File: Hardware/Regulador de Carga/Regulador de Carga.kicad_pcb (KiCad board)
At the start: 2 copper layers, 16 parts

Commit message: Actualizacion de placas
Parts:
- removed BATout1: Screw_Terminal_01x04, TerminalBlock:TerminalBlock_bornier-4_P5.08mm
- added J1: Screw_Terminal_01x05, TerminalBlock:TerminalBlock_bornier-5_P5.08mm, F.Cu at (110.5, 85.1)
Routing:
- net Net-(BATin1-Pad2): track 70.1 -> 73.4 mm
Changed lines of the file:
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@@
     (add_net "Net-(op1-Pad8)")
+  )
+  (module TerminalBlock:TerminalBlock_bornier-5_P5.08mm (layer F.Cu)
+    (at 110.49 85.09 90)
+    (descr "simple 5-pin terminal block, pitch 5.08mm, revamped version of bornier5")
+    (tags "terminal block bornier5")
+    (fp_text reference J1 (at 10.15 -4.55 90) (layer F.SilkS)
+      (effects (font (size 1 1) (thickness 0.15)))
+    )
+    (fp_text value Screw_Terminal_01x05 (at 10.15 4.6 90) (layer F.Fab)
+      (effects (font (size 1 1) (thickness 0.15)))
+    )
+    (fp_line (start 23.06 4) (end -2.74 4) (layer F.CrtYd) (width 0.05))
+    (fp_line (start 23.06 4) (end 23.06 -4) (layer F.CrtYd) (width 0.05))
+    (fp_line (start -2.74 -4) (end -2.74 4) (layer F.CrtYd) (width 0.05))
+    (fp_line (start -2.74 -4) (end 23.06 -4) (layer F.CrtYd) (width 0.05))
+    (fp_line (start -2.54 -3.81) (end -2.54 3.81) (layer F.SilkS) (width 0.12))
+    (fp_line (start 22.86 -3.81) (end 22.86 3.81) (layer F.SilkS) (width 0.12))
+    (fp_line (start -2.54 -3.81) (end 22.86 -3.81) (layer F.SilkS) (width 0.12))
+    (fp_line (start -2.54 2.54) (end 22.86 2.54) (layer F.SilkS) (width 0.12))
+    (fp_line (start -2.54 3.81) (end 22.86 3.81) (layer F.SilkS) (width 0.12))
+    (fp_line (start 22.81 -3.75) (end -2.49 -3.75) (layer F.Fab) (width 0.1))
+    (fp_line (start 22.81 3.75) (end 22.81 -3.75) (layer F.Fab) (width 0.1))
+    (fp_line (start -2.49 3.75) (end 22.81 3.75) (layer F.Fab) (width 0.1))
+    (fp_line (start -2.49 -3.75) (end -2.49 3.75) (layer F.Fab) (width 0.1))
+    (fp_line (start -2.49 2.55) (end 22.81 2.55) (layer F.Fab) (width 0.1))
+    (fp_text user %R (at 10.16 0 90) (layer F.Fab)
+      (effects (font (size 1 1) (thickness 0.15)))
+    )
+    (pad 5 thru_hole circle (at 20.32 0 90) (size 3 3) (drill 1.52) (layers *.Cu *.Mask)
+      (net 2 Earth))
+    (pad 4 thru_hole circle (at 15.24 0 90) (size 3 3) (drill 1.52) (layers *.Cu *.Mask)
+      (net 1 "Net-(BATin1-Pad2)"))
+    (pad 1 thru_hole rect (at 0 0 90) (size 3 3) (drill 1.52) (layers *.Cu *.Mask)
+      (net 2 Earth))
+    (pad 3 thru_hole circle (at 10.16 0 90) (size 3 3) (drill 1.52) (layers *.Cu *.Mask)
+      (net 1 "Net-(BATin1-Pad2)"))
+    (pad 2 thru_hole circle (at 5.08 0 90) (size 3 3) (drill 1.52) (layers *.Cu *.Mask)
+      (net 1 "Net-(BATin1-Pad2)"))
+    (model ${KISYS3DMOD}/TerminalBlock.3dshapes/TerminalBlock_bornier-5_P5.08mm.wrl
+      (offset (xyz 10.15999984741211 0 0))
+      (scale (xyz 1 1 1))
+      (rotate (xyz 0 0 0))
+    )
   )
   (module Diode_THT:D_DO-15_P12.70mm_Horizontal (layer F.Cu)
@@
     )
   )
-  (module TerminalBlock:TerminalBlock_bornier-4_P5.08mm (layer F.Cu)
-    (at 110.49 66.548 270)
-    (descr "simple 4-pin terminal block, pitch 5.08mm, revamped version of bornier4")
-    (tags "terminal block bornier4")
-    (fp_text reference BATout1 (at 19.23 0.49) (layer F.SilkS)
-      (effects (font (size 1 1) (thickness 0.15)))
-    )
-    (fp_text value Screw_Terminal_01x04 (at 7.6 3.302 270) (layer F.Fab)
-      (effects (font (size 1 1) (thickness 0.15)))
-    )
-    (fp_text user %R (at 7.62 0 270) (layer F.Fab)
-      (effects (font (size 1 1) (thickness 0.15)))
-    )
-    (fp_line (start -2.48 2.55) (end 17.72 2.55) (layer F.Fab) (width 0.1))
-    (fp_line (start -2.43 3.75) (end -2.48 3.75) (layer F.Fab) (width 0.1))
-    (fp_line (start -2.48 3.75) (end -2.48 -3.75) (layer F.Fab) (width 0.1))
-    (fp_line (start -2.48 -3.75) (end 17.72 -3.75) (layer F.Fab) (width 0.1))
-    (fp_line (start 17.72 -3.75) (end 17.72 3.75) (layer F.Fab) (width 0.1))
-    (fp_line (start 17.72 3.75) (end -2.43 3.75) (layer F.Fab) (width 0.1))
-    (fp_line (start -2.54 -3.81) (end -2.54 3.81) (layer F.SilkS) (width 0.12))
-    (fp_line (start 17.78 3.81) (end 17.78 -3.81) (layer F.SilkS) (width 0.12))
-    (fp_line (start 17.78 2.54) (end -2.54 2.54) (layer F.SilkS) (width 0.12))
-    (fp_line (start -2.54 -3.81) (end 17.78 -3.81) (layer F.SilkS) (width 0.12))
-    (fp_line (start -2.54 3.81) (end 17.78 3.81) (layer F.SilkS) (width 0.12))
-    (fp_line (start -2.73 -4) (end 17.97 -4) (layer F.CrtYd) (width 0.05))
-    (fp_line (start -2.73 -4) (end -2.73 4) (layer F.CrtYd) (width 0.05))
-    (fp_line (start 17.97 4) (end 17.97 -4) (layer F.CrtYd) (width 0.05))
-    (fp_line (start 17.97 4) (end -2.73 4) (layer F.CrtYd) (width 0.05))
-    (pad 2 thru_hole circle (at 5.08 0 270) (size 3 3) (drill 1.52) (layers *.Cu *.Mask)
-      (net 1 "Net-(BATin1-Pad2)"))
-    (pad 3 thru_hole circle (at 10.16 0 270) (size 3 3) (drill 1.52) (layers *.Cu *.Mask)
-      (net 1 "Net-(BATin1-Pad2)"))
-    (pad 1 thru_hole rect (at 0 0 270) (size 3 3) (drill 1.52) (layers *.Cu *.Mask)
-      (net 2 Earth))
-    (pad 4 thru_hole circle (at 15.24 0 270) (size 3 3) (drill 1.52) (layers *.Cu *.Mask)
-      (net 2 Earth))
-    (model ${KISYS3DMOD}/TerminalBlock.3dshapes/TerminalBlock_bornier-4_P5.08mm.wrl
-      (offset (xyz 7.619999885559082 0 0))
-      (scale (xyz 1 1 1))
-      (rotate (xyz 0 0 0))
-    )
-  )
   (module Resistor_THT:R_Axial_DIN0204_L3.6mm_D1.6mm_P7.62mm_Horizontal (layer F.Cu)
     (at 128.016 73.152 90)
@@
   (segment (start 117 81) (end 118.13137 81) (width 1) (layer B.Cu) (net 1))
   (segment (start 125.476 86.36) (end 128.524 86.36) (width 1) (layer B.Cu) (net 1))
-  (segment (start 117.602 76.708) (end 118.11 76.2) (width 1) (layer B.Cu) (net 1))
-  (segment (start 110.49 76.708) (end 117.602 76.708) (width 1) (layer B.Cu) (net 1))
-  (segment (start 110.49 76.708) (end 110.49 71.628) (width 1) (layer B.Cu) (net 1))
-  (segment (start 118.11 65.278) (end 118.11 65.024) (width 1) (layer B.Cu) (net 1))
-  (segment (start 110.49 71.628) (end 111.76 71.628) (width 1) (layer B.Cu) (net 1))
-  (segment (start 111.76 71.628) (end 118.11 65.278) (width 1) (layer B.Cu) (net 1))
   (segment (start 142.748 62.484) (end 143.256 62.992) (width 1) (layer B.Cu) (net 1))
   (segment (start 142.24 61.976) (end 143.256 62.992) (width 1) (layer B.Cu) (net 1))
@@
   (segment (start 118.11 65.024) (end 118.11 64.77) (width 1) (layer B.Cu) (net 1))
   (segment (start 118.11 64.77) (end 120.904 61.976) (width 1) (layer B.Cu) (net 1))
-  (via (at 138.43 71.12) (size 0.8) (drill 0.4) (layers F.Cu B.Cu) (net 5))
+  (segment (start 110.49 69.85) (end 110.49 74.93) (width 1) (layer B.Cu) (net 1))
+  (segment (start 110.49 80.01) (end 110.49 74.93) (width 1) (layer B.Cu) (net 1))
+  (segment (start 113.284 69.85) (end 118.11 65.024) (width 1) (layer B.Cu) (net 1))
+  (segment (start 110.49 69.85) (end 113.284 69.85) (width 1) (layer B.Cu) (net 1))
+  (segment (start 116.01 80.01) (end 117 81) (width 1) (layer B.Cu) (net 1))
+  (segment (start 110.49 80.01) (end 116.01 80.01) (width 1) (layer B.Cu) (net 1))
   (segment (start 124.54 77.55) (end 124.54 81.788) (width 1) (layer B.Cu) (net 3))
   (segment (start 123.19 76.2) (end 124.54 77.55) (width 1) (layer B.Cu) (net 3))
@@
   (segment (start 134.62 79.87137) (end 138.06063 83.312) (width 1) (layer B.Cu) (net 4))
   (segment (start 138.06063 83.312) (end 139.192 83.312) (width 1) (layer B.Cu) (net 4))
+  (via (at 138.43 71.12) (size 0.8) (drill 0.4) (layers F.Cu B.Cu) (net 5))
   (segment (start 154.432 72.136) (end 154.94 72.644) (width 1) (layer B.Cu) (net 8))
   (segment (start 154.432 67.056) (end 154.432 72.136) (width 1) (layer B.Cu) (net 8))

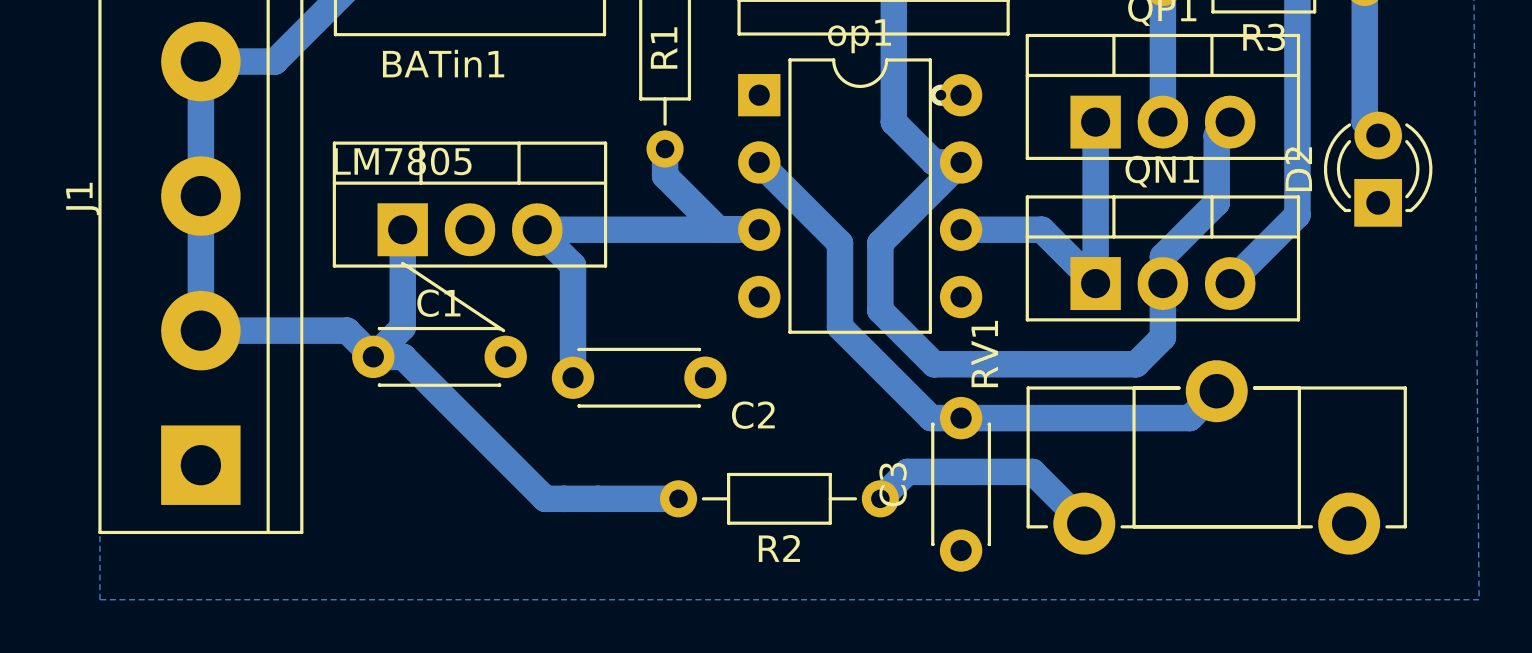
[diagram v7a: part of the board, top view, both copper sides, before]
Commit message: Preparar para impresion
Prepare todas las placas para imprimirlas
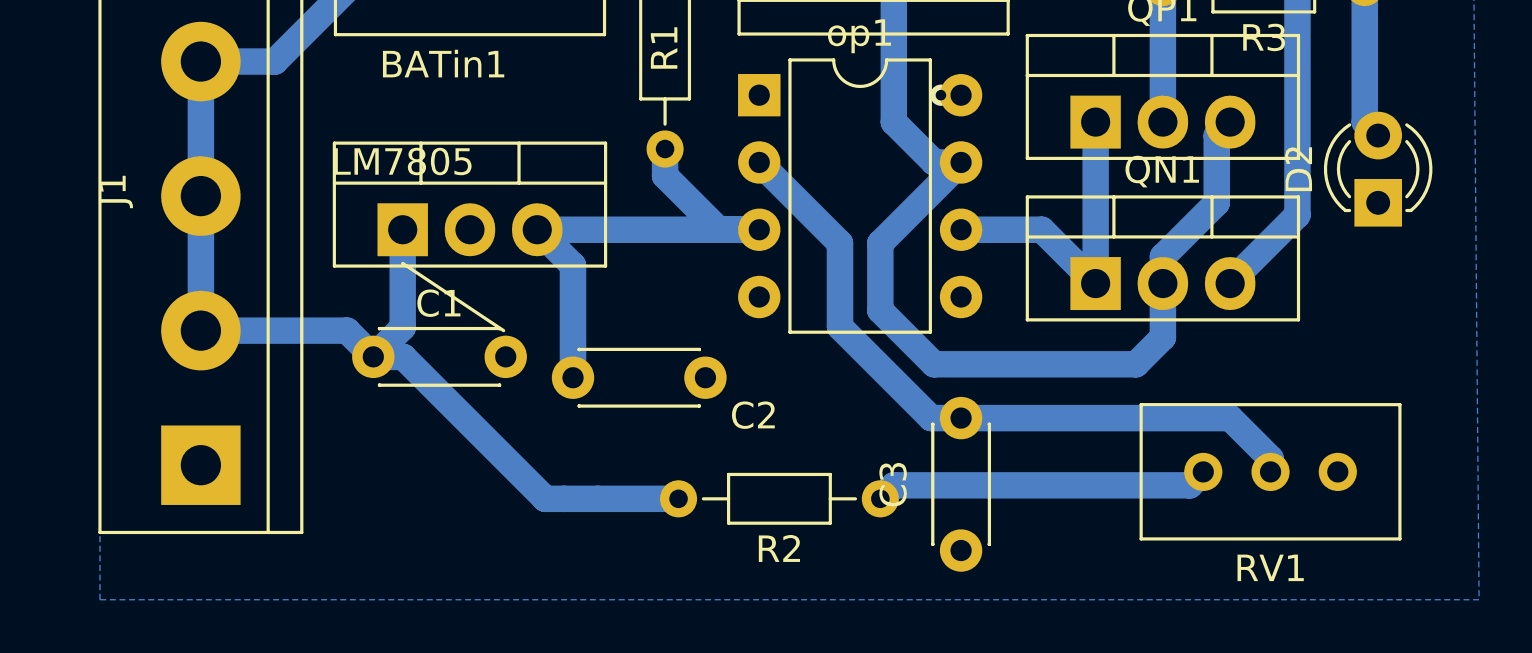
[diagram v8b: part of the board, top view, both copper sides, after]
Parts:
- RV1: footprint Potentiometer_THT:Potentiometer_ACP_CA14-H5_Horizontal -> Potentiometer_THT:Potentiometer_Bourns_3296W_Vertical
- moved RV1 4.90 mm to (148.3, 85.3), turned to 180 degrees
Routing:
- net Net-(R2-Pad1): track 8.93 -> 12.6 mm
- net Net-(C3-Pad2): track 23.5 -> 26.3 mm
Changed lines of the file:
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@@
     (thickness 1.6)
     (drawings 1)
-    (tracks 59)
+    (tracks 60)
     (zones 0)
     (modules 16)
@@
     (add_net "Net-(op1-Pad8)")
   )
+  (module Potentiometer_THT:Potentiometer_Bourns_3296W_Vertical (layer F.Cu)
+    (at 148.336 85.344 180)
+    (descr "Potentiometer, vertical, Bourns 3296W, https://www.bourns.com/pdfs/3296.pdf")
+    (tags "Potentiometer vertical Bourns 3296W")
+    (fp_text reference RV1 (at -2.54 -3.66) (layer F.SilkS)
+      (effects (font (size 1 1) (thickness 0.15)))
+    )
+    (fp_text value R_POT (at -2.54 3.67) (layer F.Fab)
+      (effects (font (size 1 1) (thickness 0.15)))
+    )
+    (fp_text user %R (at -3.175 0.005) (layer F.Fab)
+      (effects (font (size 1 1) (thickness 0.15)))
+    )
+    (fp_line (start 2.5 -2.7) (end -7.6 -2.7) (layer F.CrtYd) (width 0.05))
+    (fp_line (start 2.5 2.7) (end 2.5 -2.7) (layer F.CrtYd) (width 0.05))
+    (fp_line (start -7.6 2.7) (end 2.5 2.7) (layer F.CrtYd) (width 0.05))
+    (fp_line (start -7.6 -2.7) (end -7.6 2.7) (layer F.CrtYd) (width 0.05))
+    (fp_line (start 2.345 -2.53) (end 2.345 2.54) (layer F.SilkS) (width 0.12))
+    (fp_line (start -7.425 -2.53) (end -7.425 2.54) (layer F.SilkS) (width 0.12))
+    (fp_line (start -7.425 2.54) (end 2.345 2.54) (layer F.SilkS) (width 0.12))
+    (fp_line (start -7.425 -2.53) (end 2.345 -2.53) (layer F.SilkS) (width 0.12))
+    (fp_line (start 0.955 2.235) (end 0.956 0.066) (layer F.Fab) (width 0.1))
+    (fp_line (start 0.955 2.235) (end 0.956 0.066) (layer F.Fab) (width 0.1))
+    (fp_line (start 2.225 -2.41) (end -7.305 -2.41) (layer F.Fab) (width 0.1))
+    (fp_line (start 2.225 2.42) (end 2.225 -2.41) (layer F.Fab) (width 0.1))
+    (fp_line (start -7.305 2.42) (end 2.225 2.42) (layer F.Fab) (width 0.1))
+    (fp_line (start -7.305 -2.41) (end -7.305 2.42) (layer F.Fab) (width 0.1))
+    (fp_circle (center 0.955 1.15) (end 2.05 1.15) (layer F.Fab) (width 0.1))
+    (pad 3 thru_hole circle (at -5.08 0 180) (size 1.44 1.44) (drill 0.8) (layers *.Cu *.Mask)
+      (net 2 Earth))
+    (pad 2 thru_hole circle (at -2.54 0 180) (size 1.44 1.44) (drill 0.8) (layers *.Cu *.Mask)
+      (net 4 "Net-(C3-Pad2)"))
+    (pad 1 thru_hole circle (at 0 0 180) (size 1.44 1.44) (drill 0.8) (layers *.Cu *.Mask)
+      (net 10 "Net-(R2-Pad1)"))
+    (model ${KISYS3DMOD}/Potentiometer_THT.3dshapes/Potentiometer_Bourns_3296W_Vertical.wrl
+      (at (xyz 0 0 0))
+      (scale (xyz 1 1 1))
+      (rotate (xyz 0 0 0))
+    )
+  )
   (module TerminalBlock:TerminalBlock_bornier-5_P5.08mm (layer F.Cu)
     (at 110.49 85.09 90)
     (descr "simple 5-pin terminal block, pitch 5.08mm, revamped version of bornier5")
     (tags "terminal block bornier5")
-    (fp_text reference J1 (at 10.15 -4.55 90) (layer F.SilkS)
+    (fp_text reference J1 (at 10.414 -3.302 90) (layer F.SilkS)
       (effects (font (size 1 1) (thickness 0.15)))
     )
@@
     )
   )
-  (module Potentiometer_THT:Potentiometer_ACP_CA14-H5_Horizontal (layer F.Cu)
-    (at 143.844 87.296 90)
-    (descr "Potentiometer, horizontal, ACP CA14-H5, http://www.acptechnologies.com/wp-content/uploads/2017/10/03-ACP-CA14-CE14.pdf")
-    (tags "Potentiometer horizontal ACP CA14-H5")
-    (fp_text reference RV1 (at 6.4 -3.72 270) (layer F.SilkS)
-      (effects (font (size 1 1) (thickness 0.15)))
-    )
-    (fp_text value R_POT (at 0 13.25 270) (layer F.Fab)
-      (effects (font (size 1 1) (thickness 0.15)))
-    )
-    (fp_text user %R (at 2.5 5 270) (layer F.Fab)
-      (effects (font (size 1 1) (thickness 0.15)))
-    )
-    (fp_line (start 6.45 -2.25) (end -1.45 -2.25) (layer F.CrtYd) (width 0.05))
-    (fp_line (start 6.45 12.25) (end 6.45 -2.25) (layer F.CrtYd) (width 0.05))
-    (fp_line (start -1.45 12.25) (end 6.45 12.25) (layer F.CrtYd) (width 0.05))
-    (fp_line (start -1.45 -2.25) (end -1.45 12.25) (layer F.CrtYd) (width 0.05))
-    (fp_line (start 5.12 6.425) (end 5.12 8.121) (layer F.SilkS) (width 0.12))
-    (fp_line (start 5.12 1.88) (end 5.12 3.575) (layer F.SilkS) (width 0.12))
-    (fp_line (start -0.121 1.88) (end -0.121 8.121) (layer F.SilkS) (width 0.12))
-    (fp_line (start -0.121 8.121) (end 5.12 8.121) (layer F.SilkS) (width 0.12))
-    (fp_line (start -0.121 1.88) (end 5.12 1.88) (layer F.SilkS) (width 0.12))
-    (fp_line (start -0.121 1.426) (end -0.121 8.575) (layer F.SilkS) (width 0.12))
-    (fp_line (start -0.121 -2.12) (end -0.121 -1.426) (layer F.SilkS) (width 0.12))
-    (fp_line (start -0.121 11.425) (end -0.121 12.12) (layer F.SilkS) (width 0.12))
-    (fp_line (start 5.12 6.425) (end 5.12 12.12) (layer F.SilkS) (width 0.12))
-    (fp_line (start 5.12 -2.12) (end 5.12 3.575) (layer F.SilkS) (width 0.12))
-    (fp_line (start -0.121 12.12) (end 5.12 12.12) (layer F.SilkS) (width 0.12))
-    (fp_line (start -0.121 -2.12) (end 5.12 -2.12) (layer F.SilkS) (width 0.12))
-    (fp_line (start 5 2) (end 0 2) (layer F.Fab) (width 0.1))
-    (fp_line (start 5 8) (end 5 2) (layer F.Fab) (width 0.1))
-    (fp_line (start 0 8) (end 5 8) (layer F.Fab) (width 0.1))
-    (fp_line (start 0 2) (end 0 8) (layer F.Fab) (width 0.1))
-    (fp_line (start 0 -2) (end 5 -2) (layer F.Fab) (width 0.1))
-    (fp_line (start 0 12) (end 0 -2) (layer F.Fab) (width 0.1))
-    (fp_line (start 5 12) (end 0 12) (layer F.Fab) (width 0.1))
-    (fp_line (start 5 -2) (end 5 12) (layer F.Fab) (width 0.1))
-    (pad 1 thru_hole circle (at 0 0 90) (size 2.34 2.34) (drill 1.3) (layers *.Cu *.Mask)
-      (net 10 "Net-(R2-Pad1)"))
-    (pad 2 thru_hole circle (at 5 5 90) (size 2.34 2.34) (drill 1.3) (layers *.Cu *.Mask)
-      (net 4 "Net-(C3-Pad2)"))
-    (pad 3 thru_hole circle (at 0 10 90) (size 2.34 2.34) (drill 1.3) (layers *.Cu *.Mask)
-      (net 2 Earth))
-    (model ${KISYS3DMOD}/Potentiometer_THT.3dshapes/Potentiometer_ACP_CA14-H5_Horizontal.wrl
-      (at (xyz 0 0 0))
-      (scale (xyz 1 1 1))
-      (rotate (xyz 0 0 0))
-    )
-  )
   (module Resistor_THT:R_Axial_DIN0204_L3.6mm_D1.6mm_P7.62mm_Horizontal (layer F.Cu)
     (at 128.016 73.152 90)
@@
   (segment (start 128.016 73.152) (end 128.016 74.168) (width 1) (layer B.Cu) (net 3))
   (segment (start 128.016 74.168) (end 130.048 76.2) (width 1) (layer B.Cu) (net 3))
-  (segment (start 147.828 83.312) (end 148.844 82.296) (width 1) (layer B.Cu) (net 4))
-  (segment (start 139.192 83.312) (end 147.828 83.312) (width 1) (layer B.Cu) (net 4))
   (segment (start 134.62 76.708) (end 134.62 79.87137) (width 1) (layer B.Cu) (net 4))
   (segment (start 131.572 73.66) (end 134.62 76.708) (width 1) (layer B.Cu) (net 4))
   (segment (start 134.62 79.87137) (end 138.06063 83.312) (width 1) (layer B.Cu) (net 4))
   (segment (start 138.06063 83.312) (end 139.192 83.312) (width 1) (layer B.Cu) (net 4))
+  (segment (start 150.876 84.836) (end 150.876 85.344) (width 1) (layer B.Cu) (net 4))
+  (segment (start 139.192 83.312) (end 149.352 83.312) (width 1) (layer B.Cu) (net 4))
+  (segment (start 149.352 83.312) (end 150.876 84.836) (width 1) (layer B.Cu) (net 4))
   (via (at 138.43 71.12) (size 0.8) (drill 0.4) (layers F.Cu B.Cu) (net 5))
   (segment (start 154.432 72.136) (end 154.94 72.644) (width 1) (layer B.Cu) (net 8))
@@
   (segment (start 146.812 80.264) (end 146.812 78.232) (width 1) (layer B.Cu) (net 9))
   (segment (start 145.796 81.28) (end 146.812 80.264) (width 1) (layer B.Cu) (net 9))
-  (segment (start 141.892 85.344) (end 143.844 87.296) (width 1) (layer B.Cu) (net 10))
-  (segment (start 136.144 86.36) (end 137.16 85.344) (width 1) (layer B.Cu) (net 10))
-  (segment (start 137.16 85.344) (end 141.892 85.344) (width 1) (layer B.Cu) (net 10))
+  (segment (start 147.828 85.852) (end 148.336 85.344) (width 1) (layer B.Cu) (net 10))
+  (segment (start 136.144 86.36) (end 136.652 85.852) (width 1) (layer B.Cu) (net 10))
+  (segment (start 136.652 85.852) (end 147.828 85.852) (width 1) (layer B.Cu) (net 10))
   (segment (start 151.892 75.6445) (end 151.892 65.024) (width 1) (layer B.Cu) (net 11))
   (segment (start 149.352 78.232) (end 149.352 78.1845) (width 1) (layer B.Cu) (net 11))
